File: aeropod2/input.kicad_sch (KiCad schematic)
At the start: 5 parts, among them J2 Conn_01x18, U4 MPR121QR2

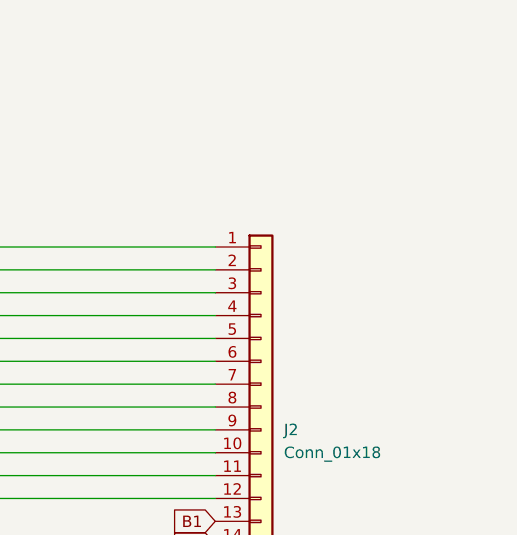
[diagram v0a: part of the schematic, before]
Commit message: Fix schematic faults found in electrical review, add reset/boot buttons
Four faults would have stopped the main board working:

- EN had no pull-up. R4/C5 sat on the unused throw of SW1 while EN was
  left holding only an AC coupled cap, so the module would not have
  booted. R4/C5 now sit on EN, and SW1/SW2 are momentary buttons to
  ground instead of slide switches.
- The microSD was miswired: connections shifted by one pin and CMD tied
  to GND, so no card could ever initialise. The display data line also
  shared a net with the card's DAT0 output. CS now lands on DAT3/CD,
  CMD on IO23 alongside the display, and IO19 is MISO from the card
  alone.
- The boost inductor was never connected to the input rail, so the
  MT3608 had nothing to pump. Rebuilt as VREGIN to L1 to SW plus diode
  anode, with the output caps and feedback divider past the diode.
- The 3.3 V rail had no headroom. R17 is now 100k, putting the boost
  near 5.1 V so the AMS1117 can actually regulate.

Also: backlight control on a new J6 pin 8 driven from IO33, 10k pull-ups
on all five button lines so GPIO35 stops floating, a 100k/100k battery
divider into IO34, both charge LEDs flipped the right way round, 33 ohm
audio series resistors instead of 470, and TP4056 set to about 400 mA.

The CP2102N auto-reset caps are gone. That package brings out RTS but no
DTR, and C30 drove IO0 from CTS, which is an input, so it could not have
worked. Flashing uses the buttons.

Firmware config.h is rewritten against the corrected schematic, and
i2s_output_init now releases the PCM5102A hardware mute on GPIO12, which
nothing was driving.

Schematic passes ERC with no new violations. The PCB has not been
re-laid-out yet, so the main board gerbers are stale; see
ELECTRICAL_REVIEW.md.
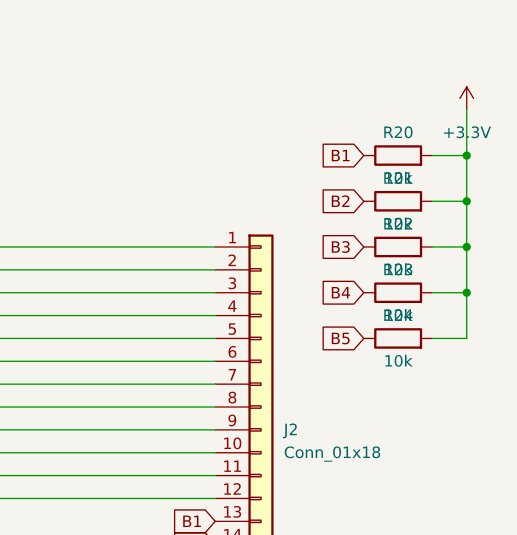
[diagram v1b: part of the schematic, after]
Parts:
- added R20, R21, R22, R23, R24: 10k, Resistor_SMD:R_0402_1005Metric, symbol Device:R
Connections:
- net +3.3V: now also R20.2, R21.2, R22.2, R23.2, R24.2
- net B1: now also R20.1
- net B2: now also R21.1
- net B3: now also R22.1
- net B4: now also R23.1
- net B5: now also R24.1

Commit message: Drop button pull-ups and backlight pin, clear ERC, vendor CP2102N footprint
The five button pull-ups are gone. The only line that actually needed one
was B5, because it sat on GPIO35 and GPIO34-39 are input only with no
internal pull-up. B5 now sits on GPIO33, a full GPIO, so the ESP32's own
pull-ups hold all five buttons high and R20-R24 are removed. GPIO35 is
spare.

The display connector goes back to seven pins. There is no backlight
control line, so the module's BL input is tied to 3.3 V and runs at full
brightness. The LEDC setup is removed and display_backlight() is a no-op
so callers do not change.

The five power_pin_not_driven errors are now properly resolved with
PWR_FLAGs on GND, VBUS, VSYS, AVDD and GNDA. To be clear about the VSS
one: that check looks for a power output pin on each rail and finds none
on a rail fed through a diode, ferrite or net tie. It was never a wiring
fault. Before the fixes it named J5 pin 3 CMD, because CMD was wrongly on
the GND net; afterwards it named J5 pin 6 VSS, which is the card's ground
pin and belongs there. The name moved because CMD left the ground net,
which is what the fix was for. Schematic is now 0 errors, 0 warnings.

The microSD wiring was re-verified pin by pin against the SD spec in SPI
mode: DAT2 and DAT1 unused, CS on DAT3/CD, MOSI on CMD, MISO on DAT0,
CLK on pin 5, VDD on pin 4, VSS on GND. All eight correct.

Footprints for every one of the 67 components were checked against what
is on disk. U6 was pointing at a vendor library in a Downloads folder
via a global nickname, so it built here and nowhere else. That library is
now vendored at aeropod2/footprints.pretty with a project fp-lib-table.

Also gitignores KiCad .lck session files.
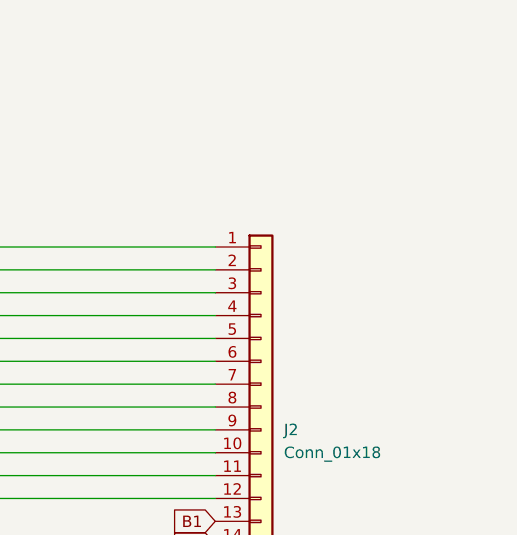
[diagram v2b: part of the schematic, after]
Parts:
- removed R20, R21, R22, R23, R24: 10k, Resistor_SMD:R_0402_1005Metric, symbol Device:R
